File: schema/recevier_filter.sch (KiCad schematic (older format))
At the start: 9 parts

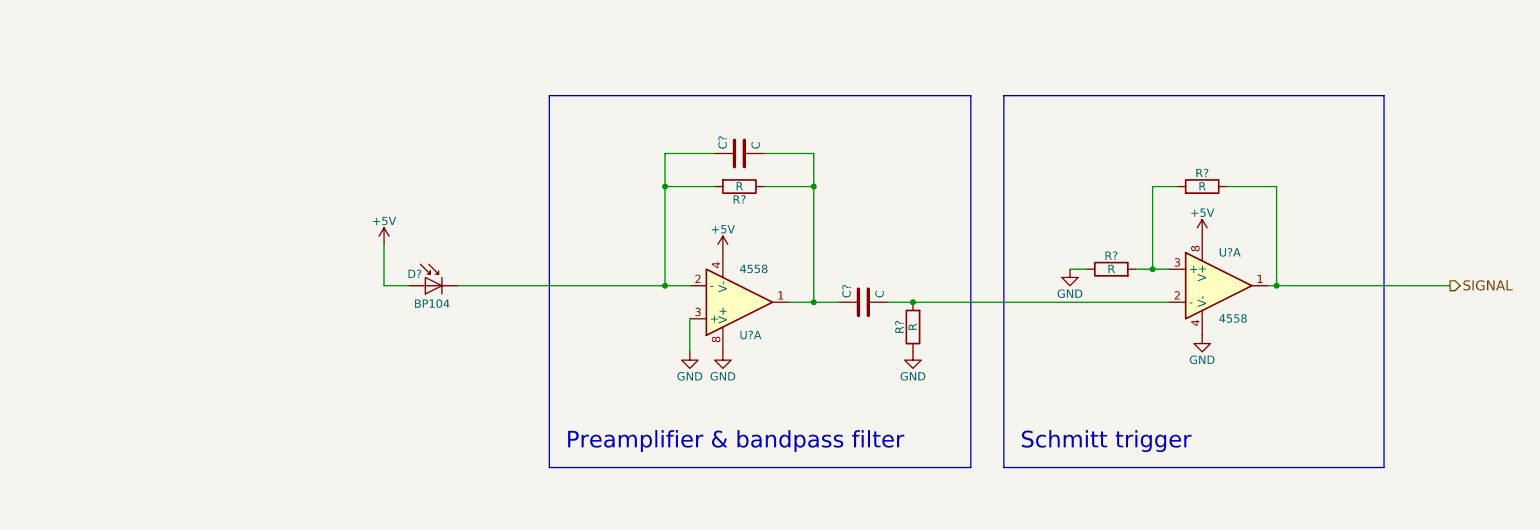
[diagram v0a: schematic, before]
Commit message: led driver MOS, correct opamp
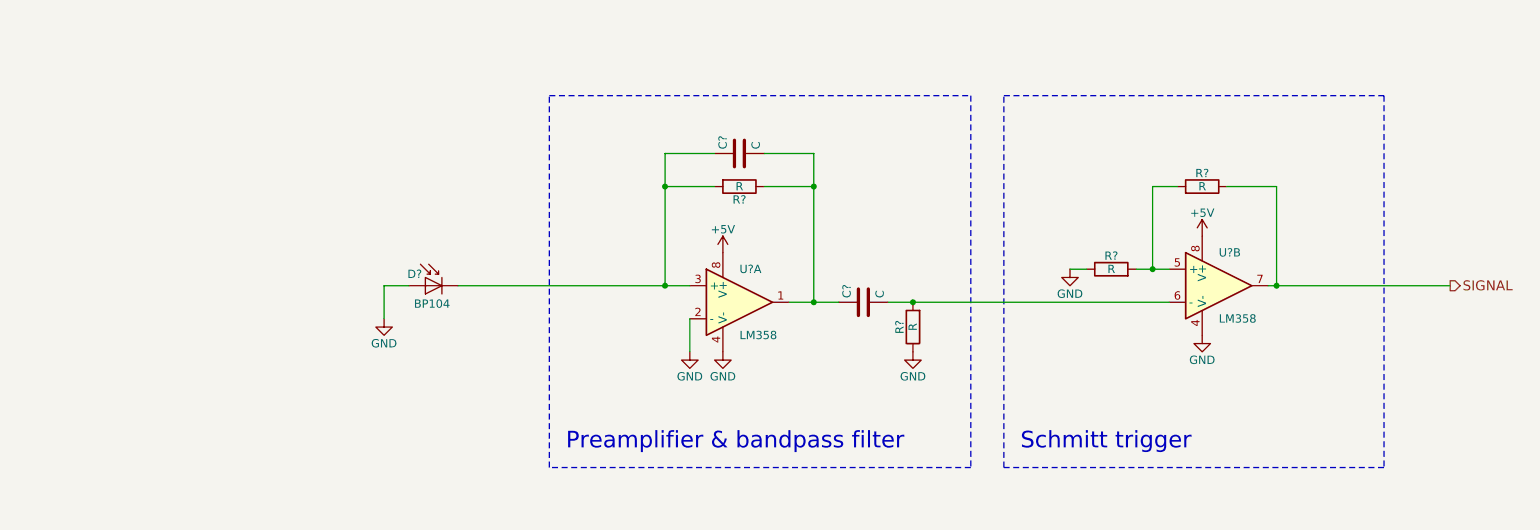
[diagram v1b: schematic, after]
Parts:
- removed U? (x2): 4558, symbol 4558
- added U? (x2): LM358, symbol LM358
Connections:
- net +5V: now also U?.8 (V+), U?.8 (V+); no longer D?.2 (A)
- net GND: now also D?.2 (A), U?.2 (-), U?.4 (V-), U?.4 (V-)
- net SIGNAL: now also U?.7
- net at C?.1, D?.1 (K), R?.2: now also U?.3 (+)
- net at C?.1, C?.2, R?.1: now also U?.1
- net at C?.2, R?.2: now also U?.6 (-)
- net at R?.2, R?.2: now also U?.5 (+)
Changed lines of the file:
@@
-$EndComp
-$Comp
-L 4558 U?
-U 1 1 591066A9
-P 5550 3350
-F 0 "U?" H 5550 3550 50  0000 L CNN
-F 1 "4558" H 5550 3150 50  0000 L CNN
-F 2 "" H 5550 3350 50  0000 C CNN
-F 3 "" H 5550 3350 50  0000 C CNN
-	1    5550 3350
-	1    0    0    1
 $EndComp
 $Comp
@@
 	3850 3250 5250 3250
 Wire Wire Line
-	3400 3250 3400 3000
+	3400 3250 3400 3450
 $Comp
 L R R?
@@
 Connection ~ 6000 2650
 $Comp
-L +5V #PWR?
-U 1 1 5910A311
-P 3400 3000
-F 0 "#PWR?" H 3400 2850 50  0001 C CNN
-F 1 "+5V" H 3400 3140 50  0000 C CNN
-F 2 "" H 3400 3000 50  0000 C CNN
-F 3 "" H 3400 3000 50  0000 C CNN
-	1    3400 3000
-	1    0    0    -1
-$EndComp
-$Comp
-L 4558 U?
-U 1 1 5910A783
-P 8450 3250
-F 0 "U?" H 8450 3450 50  0000 L CNN
-F 1 "4558" H 8450 3050 50  0000 L CNN
-F 2 "" H 8450 3250 50  0000 C CNN
-F 3 "" H 8450 3250 50  0000 C CNN
-	1    8450 3250
-	1    0    0    -1
-$EndComp
-$Comp
 L R R?
 U 1 1 5910A9B3
@@
 	1    0    0    -1
 $EndComp
-Wire Bus Line
-	7150 2100 7150 4350
-Wire Bus Line
-	7150 4350 9450 4350
-Wire Bus Line
-	9450 4350 9450 2100
-Wire Bus Line
-	9450 2100 7150 2100
-Wire Bus Line
-	6950 2100 6950 4350
-Wire Bus Line
-	6950 2100 4400 2100
-Wire Bus Line
-	4400 2100 4400 4350
-Wire Bus Line
-	4400 4350 6950 4350
 Wire Wire Line
 	3550 3250 3400 3250
@@
 Text Notes 7250 4250 0    100  ~ 0
 Schmitt trigger
+$Comp
+L GND #PWR?
+U 1 1 59131F36
+P 3400 3450
+F 0 "#PWR?" H 3400 3200 50  0001 C CNN
+F 1 "GND" H 3400 3300 50  0000 C CNN
+F 2 "" H 3400 3450 50  0000 C CNN
+F 3 "" H 3400 3450 50  0000 C CNN
+	1    3400 3450
+	1    0    0    -1
+$EndComp
+$Comp
+L LM358 U?
+U 1 1 59132113
+P 5550 3350
+F 0 "U?" H 5550 3550 50  0000 L CNN
+F 1 "LM358" H 5550 3150 50  0000 L CNN
+F 2 "" H 5550 3350 50  0000 C CNN
+F 3 "" H 5550 3350 50  0000 C CNN
+	1    5550 3350
+	1    0    0    -1
+$EndComp
+$Comp
+L LM358 U?
+U 2 1 5913218F
+P 8450 3250
+F 0 "U?" H 8450 3450 50  0000 L CNN
+F 1 "LM358" H 8450 3050 50  0000 L CNN
+F 2 "" H 8450 3250 50  0000 C CNN
+F 3 "" H 8450 3250 50  0000 C CNN
+	2    8450 3250
+	1    0    0    -1
+$EndComp
+Wire Notes Line
+	4400 2100 6950 2100
+Wire Notes Line
+	6950 2100 6950 4350
+Wire Notes Line
+	6950 4350 4400 4350
+Wire Notes Line
+	4400 4350 4400 2100
+Wire Notes Line
+	7150 4350 7150 2100
+Wire Notes Line
+	7150 2100 9450 2100
+Wire Notes Line
+	9450 2100 9450 4350
+Wire Notes Line
+	9450 4350 7150 4350
 $EndSCHEMATC

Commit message: some filter modif
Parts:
- removed C?: C, symbol C
- added C?: 10pF, symbol C
- C?: value C -> 100nF
- R?: value R -> 10kΩ
- R?: value R -> 2.7MΩ
- R?: value R -> 100kΩ
- R?: value R -> 1kΩ
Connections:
- net GND: now also U?.5 (+); no longer U?.2 (-)
- net SIGNAL: now also U?.1; no longer U?.7
- net at D?.1 (K), R?.2: now also U?.6 (-), C?.1; no longer U?.3 (+)
- net at C?.2, R?.2: now also U?.2 (-); no longer U?.6 (-)
- net at C?.1, R?.1: now also U?.7, C?.2; no longer U?.1
- net at R?.2, R?.2: now also U?.3 (+); no longer U?.5 (+)
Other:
- note added: "Amplifier & highpass"
- note added: "Preamplifier & lowpass"
- note removed: "Preamplifier & bandpass filter"
- note removed: "Schmitt trigger"
- moved on the sheet: C?, D?, R?

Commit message: filter and comparator
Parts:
- added C10: 100nF, symbol C
- added R19: 100kΩ, symbol R
- added R20, R21: 10kΩ, symbol R
- added U8: LM393, symbol LM393
- R16: renamed from R?; value 10kΩ -> 1kΩ
- gave numbers to parts that had none: 7
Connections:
- net +5V: now also R19.2, R21.1, U8.8 (V+)
- net GND: now also U7.3 (+), C10.2, R20.2, U8.4 (V-); no longer U7.5 (+)
- net SIGNAL: now also R21.2, U8.1; no longer R18.1, U7.1
- net at C8.1, D2.1 (K), R15.2: now also U7.2 (-); no longer U7.6 (-)
- net at C9.2, R16.2: now also U7.6 (-); no longer U7.2 (-)
- net at C8.2, C9.1, R15.1: now also U7.1; no longer U7.7
- net at R17.2, R18.2: now also U7.5 (+); no longer U7.3 (+)
- new net: R18.1, U7.7, U8.3 (+)
- new net: C10.1, R19.1, R20.1, U8.2 (_)
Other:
- note added: "Comparator"
- moved on the sheet: C8, C9, D2, R15, R16, R17, R18

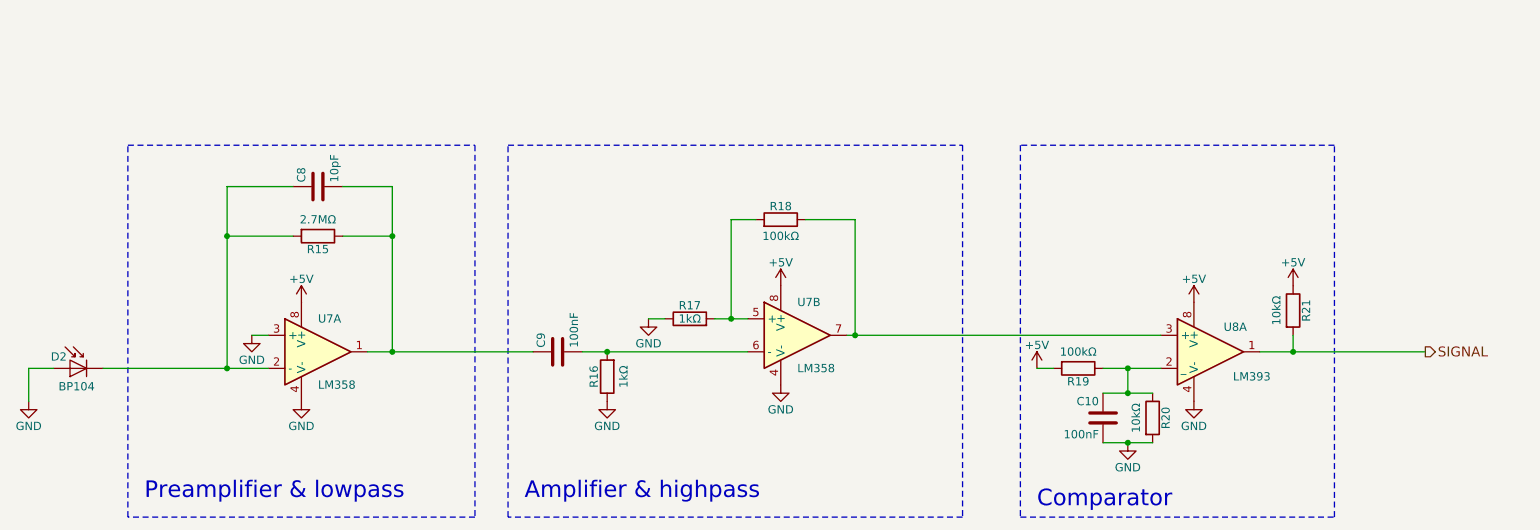
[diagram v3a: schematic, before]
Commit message: update opamp connection
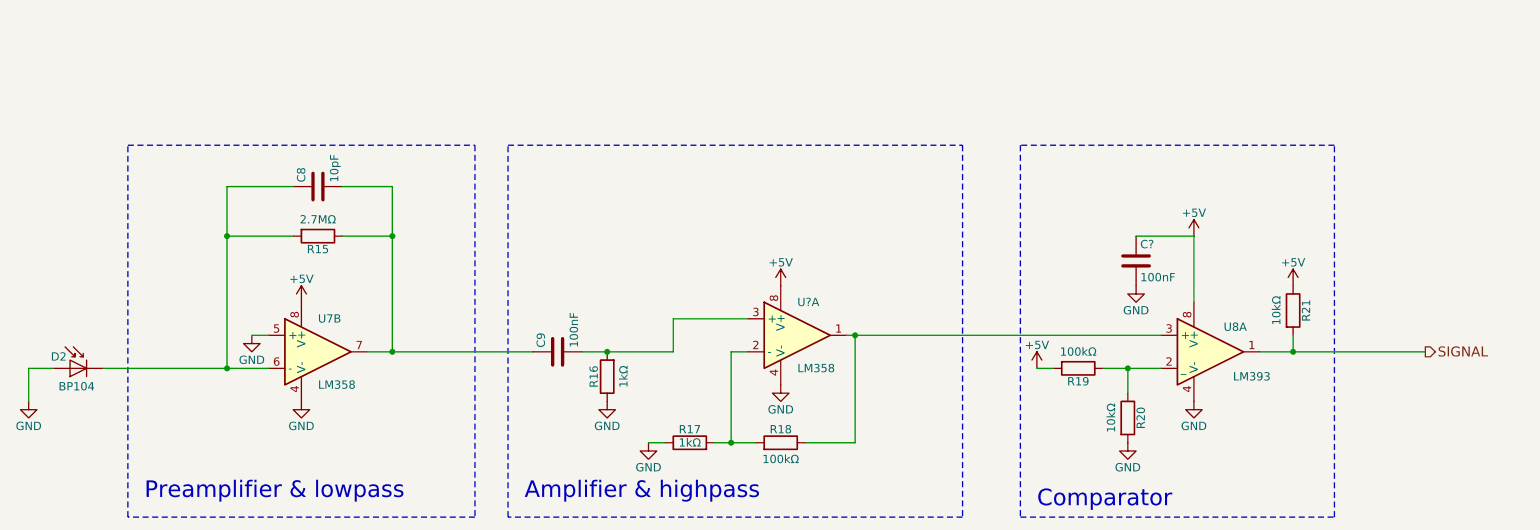
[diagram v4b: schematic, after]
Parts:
- removed C10: 100nF, symbol C
- added C?: 100nF, symbol C
- renumbered U7 to U?
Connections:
- net +5V: now also C?.1
- net GND: now also U7.5 (+), C?.2; no longer U7.3 (+)
- net at C8.1, D2.1 (K), R15.2: now also U7.6 (-); no longer U7.2 (-)
- net at C9.2, R16.2: now also U?.3 (+); no longer U?.6 (-)
- net at C8.2, C9.1, R15.1: now also U7.7; no longer U7.1
- net at R18.1, U8.3 (+): now also U?.1; no longer U?.7
- net at R17.2, R18.2: now also U?.2 (-); no longer U?.5 (+)
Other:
- moved on the sheet: R17, R18, R20
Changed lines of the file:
@@
 $EndComp
 Wire Wire Line
-	3300 3650 3450 3650
-Wire Wire Line
-	3450 3650 4300 3650
-Wire Wire Line
-	4600 3650 4750 3650
-Wire Wire Line
-	4750 3650 5600 3650
+	3300 3650 4300 3650
+Wire Wire Line
+	4600 3650 5150 3650
 Connection ~ 4750 3650
 $Comp
@@
 $EndComp
 Wire Wire Line
-	1700 3750 2450 3750
-Wire Wire Line
-	2450 3750 2700 3750
+	1700 3750 2700 3750
 Wire Wire Line
 	1250 3750 1250 3950
@@
 L R R18
 U 1 1 5910A9B3
-P 5800 2850
-F 0 "R18" V 5880 2850 50  0000 C CNN
-F 1 "100kΩ" V 5700 2850 50  0000 C CNN
-F 2 "" V 5730 2850 50  0000 C CNN
-F 3 "" H 5800 2850 50  0000 C CNN
-	1    5800 2850
+P 5800 4200
+F 0 "R18" V 5880 4200 50  0000 C CNN
+F 1 "100kΩ" V 5700 4200 50  0000 C CNN
+F 2 "" V 5730 4200 50  0000 C CNN
+F 3 "" H 5800 4200 50  0000 C CNN
+	1    5800 4200
 	0    1    -1   0
 $EndComp
@@
 L R R17
 U 1 1 5910A9E7
-P 5250 3450
-F 0 "R17" V 5330 3450 50  0000 C CNN
-F 1 "1kΩ" V 5250 3450 50  0000 C CNN
-F 2 "" V 5180 3450 50  0000 C CNN
-F 3 "" H 5250 3450 50  0000 C CNN
-	1    5250 3450
+P 5250 4200
+F 0 "R17" V 5330 4200 50  0000 C CNN
+F 1 "1kΩ" V 5250 4200 50  0000 C CNN
+F 2 "" V 5180 4200 50  0000 C CNN
+F 3 "" H 5250 4200 50  0000 C CNN
+	1    5250 4200
 	0    -1   -1   0
 $EndComp
 Wire Wire Line
-	6200 3550 6250 3550
-Wire Wire Line
-	6250 3550 8100 3550
-Wire Wire Line
-	5650 2850 5500 2850
-Wire Wire Line
-	5500 2850 5500 3450
-Wire Wire Line
-	5400 3450 5500 3450
-Wire Wire Line
-	5500 3450 5600 3450
-Connection ~ 5500 3450
-Wire Wire Line
-	5950 2850 6250 2850
-Wire Wire Line
-	6250 2850 6250 3550
+	6200 3550 8100 3550
+Wire Wire Line
+	5400 4200 5650 4200
+Connection ~ 5500 4200
+Wire Wire Line
+	5950 4200 6250 4200
+Wire Wire Line
+	6250 4200 6250 3550
 Connection ~ 6250 3550
 $Comp
 L GND #PWR19
 U 1 1 5910AC6D
-P 5000 3450
-F 0 "#PWR19" H 5000 3200 50  0001 C CNN
-F 1 "GND" H 5000 3300 50  0000 C CNN
-F 2 "" H 5000 3450 50  0000 C CNN
-F 3 "" H 5000 3450 50  0000 C CNN
-	1    5000 3450
-	1    0    0    -1
-$EndComp
-Wire Wire Line
-	5000 3450 5100 3450
+P 5000 4200
+F 0 "#PWR19" H 5000 3950 50  0001 C CNN
+F 1 "GND" H 5000 4050 50  0000 C CNN
+F 2 "" H 5000 4200 50  0000 C CNN
+F 3 "" H 5000 4200 50  0000 C CNN
+	1    5000 4200
+	1    0    0    -1
+$EndComp
+Wire Wire Line
+	5000 4200 5100 4200
 $Comp
 L +5V #PWR20
@@
 $Comp
 L LM358 U7
-U 1 1 59132113
+U 2 1 59132113
 P 3000 3650
 F 0 "U7" H 3000 3850 50  0000 L CNN
@@
 F 2 "" H 3000 3650 50  0000 C CNN
 F 3 "" H 3000 3650 50  0000 C CNN
-	1    3000 3650
-	1    0    0    -1
-$EndComp
-$Comp
-L LM358 U7
-U 2 1 5913218F
-P 5900 3550
-F 0 "U7" H 5900 3750 50  0000 L CNN
-F 1 "LM358" H 5900 3350 50  0000 L CNN
-F 2 "" H 5900 3550 50  0000 C CNN
-F 3 "" H 5900 3550 50  0000 C CNN
-	2    5900 3550
+	2    3000 3650
 	1    0    0    -1
 $EndComp
@@
 Connection ~ 2450 3750
 Wire Wire Line
-	2450 2650 2450 2950
-Wire Wire Line
-	2450 2950 2450 3750
-Wire Wire Line
-	3450 2650 3450 2950
-Wire Wire Line
-	3450 2950 3450 3650
+	2450 2650 2450 3750
+Wire Wire Line
+	3450 2650 3450 3650
 $Comp
 L C C8
@@
 L R R20
 U 1 1 5924CC6A
-P 8050 4050
-F 0 "R20" V 8130 4050 50  0000 C CNN
-F 1 "10kΩ" V 7950 4050 50  0000 C CNN
-F 2 "" V 7980 4050 50  0000 C CNN
-F 3 "" H 8050 4050 50  0000 C CNN
-	1    8050 4050
+P 7900 4050
+F 0 "R20" V 7980 4050 50  0000 C CNN
+F 1 "10kΩ" V 7800 4050 50  0000 C CNN
+F 2 "" V 7830 4050 50  0000 C CNN
+F 3 "" H 7900 4050 50  0000 C CNN
+	1    7900 4050
 	1    0    0    -1
 $EndComp
@@
 L +5V #PWR24
 U 1 1 5924CE97
-P 8300 3350
-F 0 "#PWR24" H 8300 3200 50  0001 C CNN
-F 1 "+5V" H 8300 3490 50  0000 C CNN
-F 2 "" H 8300 3350 50  0000 C CNN
-F 3 "" H 8300 3350 50  0000 C CNN
-	1    8300 3350
+P 8300 2950
+F 0 "#PWR24" H 8300 2800 50  0001 C CNN
+F 1 "+5V" H 8300 3090 50  0000 C CNN
+F 2 "" H 8300 2950 50  0000 C CNN
+F 3 "" H 8300 2950 50  0000 C CNN
+	1    8300 2950
 	1    0    0    -1
 $EndComp
@@
 	7350 3750 7450 3750
 Wire Wire Line
-	7750 3750 7900 3750
-Wire Wire Line
-	7900 3750 8100 3750
+	7750 3750 8100 3750
 Wire Wire Line
 	7900 3900 7900 3750
 Connection ~ 7900 3750
 Wire Wire Line
-	8700 3650 8900 3650
-Wire Wire Line
-	8900 3650 9700 3650
+	8700 3650 9700 3650
 Wire Notes Line
 	7250 2400 7250 4650
@@
 $EndComp
 $Comp
-L C C10
-U 1 1 5924E122
-P 7750 4050
-F 0 "C10" H 7775 4150 50  0000 L CNN
-F 1 "100nF" H 7775 3950 50  0000 L CNN
-F 2 "" H 7788 3900 50  0000 C CNN
-F 3 "" H 7750 4050 50  0000 C CNN
-	1    7750 4050
-	-1   0    0    -1
-$EndComp
-Wire Wire Line
-	7750 3900 7900 3900
-Wire Wire Line
-	7900 3900 8050 3900
-Wire Wire Line
-	7750 4200 7900 4200
-Wire Wire Line
-	7900 4200 8050 4200
-Connection ~ 7900 4200
-Connection ~ 7900 3900
+L LM358 U?
+U 1 1 5913218F
+P 5900 3550
+F 0 "U?" H 5900 3750 50  0000 L CNN
+F 1 "LM358" H 5900 3350 50  0000 L CNN
+F 2 "" H 5900 3550 50  0000 C CNN
+F 3 "" H 5900 3550 50  0000 C CNN
+	1    5900 3550
+	1    0    0    -1
+$EndComp
+Wire Wire Line
+	5600 3450 5150 3450
+Wire Wire Line
+	5600 3650 5500 3650
+Wire Wire Line
+	5500 3650 5500 4200
+Wire Wire Line
+	5150 3450 5150 3650
+$Comp
+L C C?
+U 1 1 59253FAB
+P 7950 3100
+F 0 "C?" H 7975 3200 50  0000 L CNN
+F 1 "100nF" H 7975 3000 50  0000 L CNN
+F 2 "" H 7988 2950 50  0000 C CNN
+F 3 "" H 7950 3100 50  0000 C CNN
+	1    7950 3100
+	1    0    0    -1
+$EndComp
+$Comp
+L GND #PWR?
+U 1 1 5925407F
+P 7950 3250
+F 0 "#PWR?" H 7950 3000 50  0001 C CNN
+F 1 "GND" H 7950 3100 50  0000 C CNN
+F 2 "" H 7950 3250 50  0000 C CNN
+F 3 "" H 7950 3250 50  0000 C CNN
+	1    7950 3250
+	1    0    0    -1
+$EndComp
+Wire Wire Line
+	7950 2950 8300 2950
+Wire Wire Line
+	8300 2950 8300 3350
 $EndSCHEMATC
